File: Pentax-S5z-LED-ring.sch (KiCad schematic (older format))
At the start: 0 parts

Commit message: Placed a few traces.
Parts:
- added D1, D10, D11, D12, D13, D14, D15, D16, D2, D3, D4, D5, D6, D7, D8, D9: LED, symbol LED
- added R1, R10, R11, R12, R13, R14, R15, R16, R2, R3, R4, R5, R6, R7, R8, R9: 10R, symbol R
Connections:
- new net: D1.1 (A), D10.1 (A), D11.1 (A), D12.1 (A), D13.1 (A), D14.1 (A), D15.1 (A), D16.1 (A), D2.1 (A), D3.1 (A), D4.1 (A), D5.1 (A), D6.1 (A), D7.1 (A), D8.1 (A), D9.1 (A)
- new net: D1.2 (K), R1.1
- new net: D2.2 (K), R2.1
- new net: D3.2 (K), R3.1
- new net: D4.2 (K), R4.1
- new net: R1.2, R10.2, R11.2, R12.2, R13.2, R14.2, R15.2, R16.2, R2.2, R3.2, R4.2, R5.2, R6.2, R7.2, R8.2, R9.2
- new net: D5.2 (K), R5.1
- new net: D6.2 (K), R6.1
- new net: D7.2 (K), R7.1
- new net: D8.2 (K), R8.1
- new net: D9.2 (K), R9.1
- new net: D10.2 (K), R10.1
- new net: D11.2 (K), R11.1
- new net: D12.2 (K), R12.1
- new net: D13.2 (K), R13.1
- new net: D14.2 (K), R14.1
- new net: D15.2 (K), R15.1
- new net: D16.2 (K), R16.1

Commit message: Trying to build a controller board.
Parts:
- added IC1: ATTINY13-S, SO8-200, symbol ATTINY13-S
- added JP1: MADW__AVR_ISP, ~, symbol MADW__AVR_ISP
- added Q1: MOSFET_N, ~, symbol MOSFET_N
- added R17: 150R, symbol R
- added R18: 100k, symbol R
- added SW1, SW2: SW_PUSH, symbol SW_PUSH
- R1: value 10R -> 60R
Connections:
- net +5V: now reaches D1.1 (A), D10.1 (A), D11.1 (A), D12.1 (A), D13.1 (A), D14.1 (A), D15.1 (A), D16.1 (A), D2.1 (A), D3.1 (A), D4.1 (A), D5.1 (A), D6.1 (A), D7.1 (A), D8.1 (A), D9.1 (A)
- net +5V: now also IC1.8 (VCC), JP1.2 (VTG)
- net at R1.2, R10.2, R11.2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: now also Q1.3 (D)
- new net: Q1.1 (G), R17.2, R18.1
- new net GND: IC1.4 (GND), JP1.6 (GND), Q1.2 (S), R18.2, SW1.1, SW2.1
- new net MISO: IC1.6 (PB1(MISO/AIN1/OC0B/INT0/PCINT1)), JP1.1 (MISO), SW1.2
- new net PWM: IC1.5 (PB0(MOSI/AIN0/OC0A/PCINT0)), JP1.4 (MOSI), R17.1
- new net RESET: IC1.1 (PB5(~RESET~/ADC0/PCINT5/dW)), JP1.5 (RST)
- new net SCK: IC1.7 (PB2(SCK/ADC1/T0/PCINT2)), JP1.3 (SCK), SW2.2
- no-connect marks 0 -> 2
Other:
- moved on the sheet: D1, D10, D11, D12, D13, D14, D15, D16, D2, D3, D4, D5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

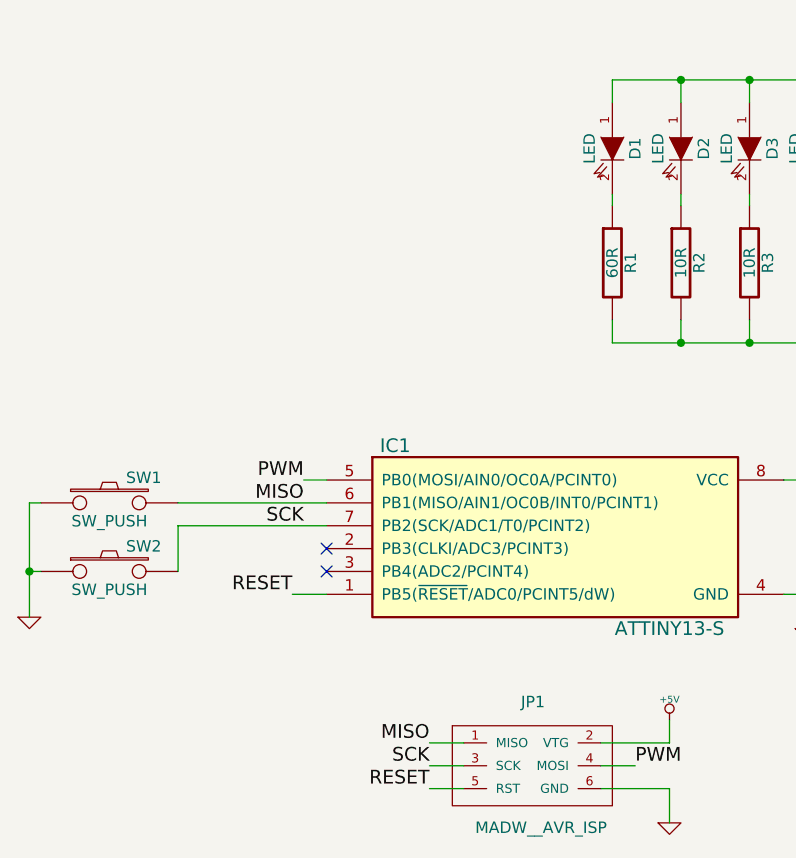
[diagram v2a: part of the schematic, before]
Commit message: Added proper SMD push-buttons.
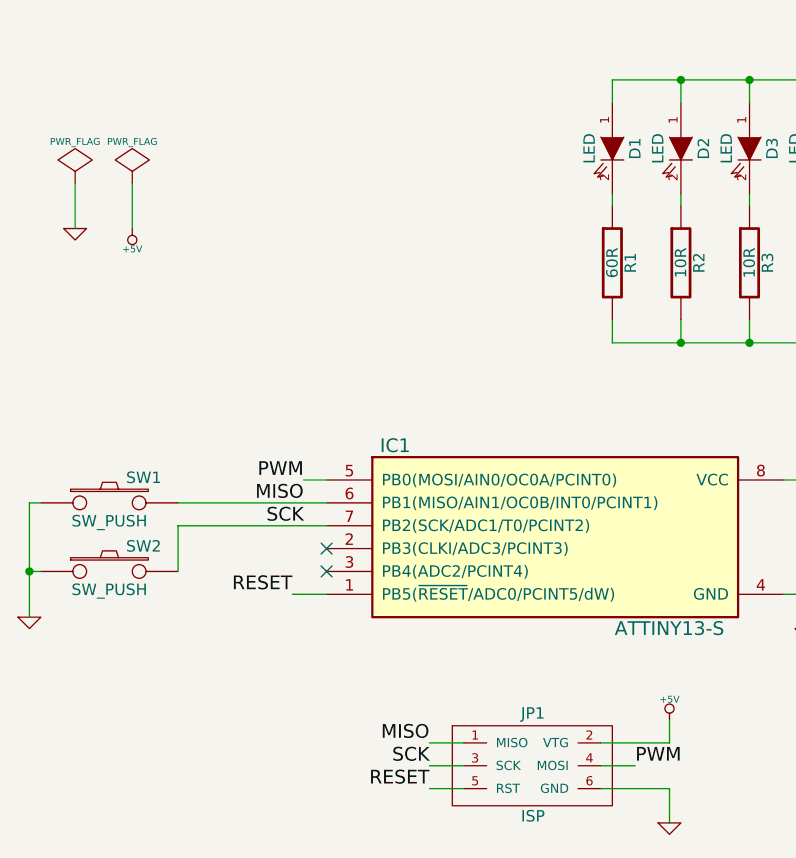
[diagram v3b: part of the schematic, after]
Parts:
- JP1: value MADW__AVR_ISP -> ISP
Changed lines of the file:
@@
-EESchema Schematic File Version 2  date Tue 09 Apr 2013 03:14:07 PM CEST
+EESchema Schematic File Version 2  date Tue 09 Apr 2013 06:31:30 PM CEST
 LIBS:my_parts
 LIBS:power
@@
 U 1 1 5164175A
 P 3200 5450
-F 0 "JP1" H 3150 5700 50  0000 L BNN
-F 1 "MADW__AVR_ISP" H 2950 5150 50  0000 L BNN
+F 0 "JP1" H 3150 5650 50  0000 L BNN
+F 1 "ISP" H 3150 5200 50  0000 L BNN
 F 2 "~" H 3200 5450 60  0000 C CNN
 F 3 "~" H 3200 5450 60  0000 C CNN
@@
 NoConn ~ 2300 4500
 NoConn ~ 2300 4600
+$Comp
+L GND #PWR09
+U 1 1 51644384
+P 1200 3100
+F 0 "#PWR09" H 1200 3100 30  0001 C CNN
+F 1 "GND" H 1200 3030 30  0001 C CNN
+F 2 "" H 1200 3100 60  0000 C CNN
+F 3 "" H 1200 3100 60  0000 C CNN
+	1    1200 3100
+	1    0    0    -1
+$EndComp
+$Comp
+L +5V #PWR010
+U 1 1 51644393
+P 1450 3100
+F 0 "#PWR010" H 1450 3190 20  0001 C CNN
+F 1 "+5V" H 1450 3190 30  0000 C CNN
+F 2 "" H 1450 3100 60  0000 C CNN
+F 3 "" H 1450 3100 60  0000 C CNN
+	1    1450 3100
+	-1   0    0    1
+$EndComp
+$Comp
+L PWR_FLAG #FLG011
+U 1 1 516443A2
+P 1200 2900
+F 0 "#FLG011" H 1200 2995 30  0001 C CNN
+F 1 "PWR_FLAG" H 1200 3080 30  0000 C CNN
+F 2 "" H 1200 2900 60  0000 C CNN
+F 3 "" H 1200 2900 60  0000 C CNN
+	1    1200 2900
+	1    0    0    -1
+$EndComp
+$Comp
+L PWR_FLAG #FLG012
+U 1 1 516443B1
+P 1450 2900
+F 0 "#FLG012" H 1450 2995 30  0001 C CNN
+F 1 "PWR_FLAG" H 1450 3080 30  0000 C CNN
+F 2 "" H 1450 2900 60  0000 C CNN
+F 3 "" H 1450 2900 60  0000 C CNN
+	1    1450 2900
+	1    0    0    -1
+$EndComp
+Wire Wire Line
+	1450 2900 1450 3100
+Wire Wire Line
+	1200 2900 1200 3100
 $EndSCHEMATC

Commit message: ...
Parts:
- added P1, P4: CONN_2, symbol CONN_2
- added P2: +, symbol CONN_1
- added P3: -, symbol CONN_1
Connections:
- net +5V: now also P1.1 (P1), P4.1 (P1); no longer D1.1 (A), D10.1 (A), D11.1 (A), D12.1 (A), D13.1 (A), D14.1 (A), D15.1 (A), D16.1 (A), D2.1 (A), D3.1 (A), D4.1 (A), D5.1 (A), D6.1 (A), D7.1 (A), D8.1 (A), D9.1 (A)
- net GND: now also P1.2 (PM)
- net at R1.2, R10.2, R11.2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: now also P3.1; no longer Q1.3 (D)
- new net: D1.1 (A), D10.1 (A), D11.1 (A), D12.1 (A), D13.1 (A), D14.1 (A), D15.1 (A), D16.1 (A), D2.1 (A), D3.1 (A), D4.1 (A), D5.1 (A), D6.1 (A), D7.1 (A), D8.1 (A), D9.1 (A), P2.1
- new net: P4.2 (PM), Q1.3 (D)
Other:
- note added: "To LED board"
- note added: "To power supply"
- moved on the sheet: D1, D10, D11, D12, D13, D14, D15, D16, D2, D3, D4, D5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

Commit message: Getting there...
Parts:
- added C1: 4.7µF, symbol C
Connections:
- net +5V: now also C1.1
- net GND: now also C1.2
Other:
- moved on the sheet: P1, P4, Q1, R17, R18
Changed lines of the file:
@@
-EESchema Schematic File Version 2  date Tue 09 Apr 2013 09:44:23 PM CEST
+EESchema Schematic File Version 2  date Wed 10 Apr 2013 12:16:09 AM CEST
 LIBS:my_parts
 LIBS:power
@@
 L R R17
 U 1 1 51640F23
-P 5150 4450
-F 0 "R17" V 5230 4450 50  0000 C CNN
-F 1 "150R" V 5150 4450 50  0000 C CNN
-F 2 "" H 5150 4450 60  0000 C CNN
-F 3 "" H 5150 4450 60  0000 C CNN
-	1    5150 4450
+P 6000 4450
+F 0 "R17" V 6080 4450 50  0000 C CNN
+F 1 "150R" V 6000 4450 50  0000 C CNN
+F 2 "" H 6000 4450 60  0000 C CNN
+F 3 "" H 6000 4450 60  0000 C CNN
+	1    6000 4450
 	0    -1   -1   0
 $EndComp
@@
 L R R18
 U 1 1 51640F32
-P 5450 4900
-F 0 "R18" V 5530 4900 50  0000 C CNN
-F 1 "100k" V 5450 4900 50  0000 C CNN
-F 2 "" H 5450 4900 60  0000 C CNN
-F 3 "" H 5450 4900 60  0000 C CNN
-	1    5450 4900
+P 6300 4900
+F 0 "R18" V 6380 4900 50  0000 C CNN
+F 1 "100k" V 6300 4900 50  0000 C CNN
+F 2 "" H 6300 4900 60  0000 C CNN
+F 3 "" H 6300 4900 60  0000 C CNN
+	1    6300 4900
 	1    0    0    -1
 $EndComp
@@
 L MOSFET_N Q1
 U 1 1 51640F6E
-P 5500 4450
-F 0 "Q1" H 5700 4740 60  0000 R CNN
-F 1 "MOSFET_N" H 5700 4350 60  0000 R CNN
-F 2 "~" H 5500 4450 60  0000 C CNN
-F 3 "~" H 5500 4450 60  0000 C CNN
-	1    5500 4450
-	1    0    0    -1
-$EndComp
-Wire Wire Line
-	5400 4450 5500 4450
-Wire Wire Line
-	5450 4450 5450 4650
-Connection ~ 5450 4450
+P 6350 4450
+F 0 "Q1" H 6550 4740 60  0000 R CNN
+F 1 "MOSFET_N" H 6550 4350 60  0000 R CNN
+F 2 "~" H 6350 4450 60  0000 C CNN
+F 3 "~" H 6350 4450 60  0000 C CNN
+	1    6350 4450
+	1    0    0    -1
+$EndComp
+Wire Wire Line
+	6250 4450 6350 4450
+Wire Wire Line
+	6300 4450 6300 4650
+Connection ~ 6300 4450
 $Comp
 L GND #PWR01
 U 1 1 51641037
-P 5450 5250
-F 0 "#PWR01" H 5450 5250 30  0001 C CNN
-F 1 "GND" H 5450 5180 30  0001 C CNN
-F 2 "" H 5450 5250 60  0000 C CNN
-F 3 "" H 5450 5250 60  0000 C CNN
-	1    5450 5250
-	1    0    0    -1
-$EndComp
-Wire Wire Line
-	5450 5150 5450 5250
-Wire Wire Line
-	5800 4550 5800 5250
+P 6300 5250
+F 0 "#PWR01" H 6300 5250 30  0001 C CNN
+F 1 "GND" H 6300 5180 30  0001 C CNN
+F 2 "" H 6300 5250 60  0000 C CNN
+F 3 "" H 6300 5250 60  0000 C CNN
+	1    6300 5250
+	1    0    0    -1
+$EndComp
+Wire Wire Line
+	6300 5150 6300 5250
+Wire Wire Line
+	6650 4550 6650 5250
 $Comp
 L GND #PWR02
 U 1 1 51641142
-P 5800 5250
-F 0 "#PWR02" H 5800 5250 30  0001 C CNN
-F 1 "GND" H 5800 5180 30  0001 C CNN
-F 2 "" H 5800 5250 60  0000 C CNN
-F 3 "" H 5800 5250 60  0000 C CNN
-	1    5800 5250
+P 6650 5250
+F 0 "#PWR02" H 6650 5250 30  0001 C CNN
+F 1 "GND" H 6650 5180 30  0001 C CNN
+F 2 "" H 6650 5250 60  0000 C CNN
+F 3 "" H 6650 5250 60  0000 C CNN
+	1    6650 5250
 	1    0    0    -1
 $EndComp
@@
 $EndComp
 Wire Wire Line
-	4300 4200 4400 4200
-Wire Wire Line
-	4400 4200 4400 4100
+	4400 4100 4400 4250
 $Comp
 L GND #PWR05
@@
 $EndComp
 Wire Wire Line
-	4300 4700 4400 4700
-Wire Wire Line
-	4400 4700 4400 4850
-Text Label 4800 4450 2    60   ~ 0
+	4400 4650 4400 4850
+Text Label 5650 4450 2    60   ~ 0
 PWM
 Wire Wire Line
-	4800 4450 4900 4450
+	5650 4450 5750 4450
 Text Label 2200 4200 2    60   ~ 0
 PWM
@@
 L GND #PWR09
 U 1 1 51644384
-P 6850 4800
-F 0 "#PWR09" H 6850 4800 30  0001 C CNN
-F 1 "GND" H 6850 4730 30  0001 C CNN
-F 2 "" H 6850 4800 60  0000 C CNN
-F 3 "" H 6850 4800 60  0000 C CNN
-	1    6850 4800
+P 5250 6250
+F 0 "#PWR09" H 5250 6250 30  0001 C CNN
+F 1 "GND" H 5250 6180 30  0001 C CNN
+F 2 "" H 5250 6250 60  0000 C CNN
+F 3 "" H 5250 6250 60  0000 C CNN
+	1    5250 6250
 	1    0    0    -1
 $EndComp
@@
 L +5V #PWR010
 U 1 1 51644393
-P 7100 4800
-F 0 "#PWR010" H 7100 4890 20  0001 C CNN
-F 1 "+5V" H 7100 4890 30  0000 C CNN
-F 2 "" H 7100 4800 60  0000 C CNN
-F 3 "" H 7100 4800 60  0000 C CNN
-	1    7100 4800
+P 5500 6250
+F 0 "#PWR010" H 5500 6340 20  0001 C CNN
+F 1 "+5V" H 5500 6340 30  0000 C CNN
+F 2 "" H 5500 6250 60  0000 C CNN
+F 3 "" H 5500 6250 60  0000 C CNN
+	1    5500 6250
 	-1   0    0    1
 $EndComp
@@
 L PWR_FLAG #FLG011
 U 1 1 516443A2
-P 6850 4600
-F 0 "#FLG011" H 6850 4695 30  0001 C CNN
-F 1 "PWR_FLAG" H 6850 4780 30  0000 C CNN
-F 2 "" H 6850 4600 60  0000 C CNN
-F 3 "" H 6850 4600 60  0000 C CNN
-	1    6850 4600
+P 5250 6050
+F 0 "#FLG011" H 5250 6145 30  0001 C CNN
+F 1 "PWR_FLAG" H 5250 6230 30  0000 C CNN
+F 2 "" H 5250 6050 60  0000 C CNN
+F 3 "" H 5250 6050 60  0000 C CNN
+	1    5250 6050
 	1    0    0    -1
 $EndComp
@@
 L PWR_FLAG #FLG012
 U 1 1 516443B1
-P 7100 4600
-F 0 "#FLG012" H 7100 4695 30  0001 C CNN
-F 1 "PWR_FLAG" H 7100 4780 30  0000 C CNN
-F 2 "" H 7100 4600 60  0000 C CNN
-F 3 "" H 7100 4600 60  0000 C CNN
-	1    7100 4600
-	1    0    0    -1
-$EndComp
-Wire Wire Line
-	7100 4600 7100 4800
-Wire Wire Line
-	6850 4600 6850 4800
+P 5500 6050
+F 0 "#FLG012" H 5500 6145 30  0001 C CNN
+F 1 "PWR_FLAG" H 5500 6230 30  0000 C CNN
+F 2 "" H 5500 6050 60  0000 C CNN
+F 3 "" H 5500 6050 60  0000 C CNN
+	1    5500 6050
+	1    0    0    -1
+$EndComp
+Wire Wire Line
+	5500 6050 5500 6250
+Wire Wire Line
+	5250 6050 5250 6250
 $Comp
 L CONN_2 P1
 U 1 1 51646D70
-P 7850 4550
-F 0 "P1" V 7800 4550 40  0000 C CNN
-F 1 "CONN_2" V 7900 4550 40  0000 C CNN
-F 2 "" H 7850 4550 60  0000 C CNN
-F 3 "" H 7850 4550 60  0000 C CNN
-	1    7850 4550
+P 6250 6000
+F 0 "P1" V 6200 6000 40  0000 C CNN
+F 1 "CONN_2" V 6300 6000 40  0000 C CNN
+F 2 "" H 6250 6000 60  0000 C CNN
+F 3 "" H 6250 6000 60  0000 C CNN
+	1    6250 6000
 	0    -1   -1   0
 $EndComp
@@
 L GND #PWR013
 U 1 1 51646D84
-P 7950 5000
-F 0 "#PWR013" H 7950 5000 30  0001 C CNN
-F 1 "GND" H 7950 4930 30  0001 C CNN
-F 2 "" H 7950 5000 60  0000 C CNN
-F 3 "" H 7950 5000 60  0000 C CNN
-	1    7950 5000
+P 6350 6450
+F 0 "#PWR013" H 6350 6450 30  0001 C CNN
+F 1 "GND" H 6350 6380 30  0001 C CNN
+F 2 "" H 6350 6450 60  0000 C CNN
+F 3 "" H 6350 6450 60  0000 C CNN
+	1    6350 6450
 	1    0    0    -1
 $EndComp
@@
 L +5V #PWR014
 U 1 1 51646D93
-P 7750 5000
-F 0 "#PWR014" H 7750 5090 20  0001 C CNN
-F 1 "+5V" H 7750 5090 30  0000 C CNN
-F 2 "" H 7750 5000 60  0000 C CNN
-F 3 "" H 7750 5000 60  0000 C CNN
-	1    7750 5000
+P 6150 6450
+F 0 "#PWR014" H 6150 6540 20  0001 C CNN
+F 1 "+5V" H 6150 6540 30  0000 C CNN
+F 2 "" H 6150 6450 60  0000 C CNN
+F 3 "" H 6150 6450 60  0000 C CNN
+	1    6150 6450
 	-1   0    0    1
 $EndComp
 Wire Wire Line
-	7750 4900 7750 5000
-Wire Wire Line
-	7950 4900 7950 5000
+	6150 6350 6150 6450
+Wire Wire Line
+	6350 6350 6350 6450
 $Comp
 L CONN_1 P2
@@
 L CONN_2 P4
 U 1 1 51647217
-P 6150 3800
-F 0 "P4" V 6100 3800 40  0000 C CNN
-F 1 "CONN_2" V 6200 3800 40  0000 C CNN
-F 2 "" H 6150 3800 60  0000 C CNN
-F 3 "" H 6150 3800 60  0000 C CNN
-	1    6150 3800
-	1    0    0    -1
-$EndComp
-Wire Wire Line
-	5800 3900 5800 4150
+P 7000 3800
+F 0 "P4" V 6950 3800 40  0000 C CNN
+F 1 "CONN_2" V 7050 3800 40  0000 C CNN
+F 2 "" H 7000 3800 60  0000 C CNN
+F 3 "" H 7000 3800 60  0000 C CNN
+	1    7000 3800
+	1    0    0    -1
+$EndComp
+Wire Wire Line
+	6650 3900 6650 4150
 $Comp
 L +5V #PWR?
 U 1 1 516472A6
-P 5800 3650
-F 0 "#PWR?" H 5800 3740 20  0001 C CNN
-F 1 "+5V" H 5800 3740 30  0000 C CNN
-F 2 "" H 5800 3650 60  0000 C CNN
-F 3 "" H 5800 3650 60  0000 C CNN
-	1    5800 3650
-	1    0    0    -1
-$EndComp
-Wire Wire Line
-	5800 3650 5800 3700
-Text Notes 8100 4600 0    60   ~ 0
+P 6650 3650
+F 0 "#PWR?" H 6650 3740 20  0001 C CNN
+F 1 "+5V" H 6650 3740 30  0000 C CNN
+F 2 "" H 6650 3650 60  0000 C CNN
+F 3 "" H 6650 3650 60  0000 C CNN
+	1    6650 3650
+	1    0    0    -1
+$EndComp
+Wire Wire Line
+	6650 3650 6650 3700
+Text Notes 6500 6050 0    60   ~ 0
 To power supply
-Text Notes 6300 3850 0    60   ~ 0
+Text Notes 7150 3850 0    60   ~ 0
 To LED board
+Connection ~ 4400 4200
+Connection ~ 4400 4700
+$Comp
+L C C1
+U 1 1 516492F3
+P 4400 4450
+F 0 "C1" H 4450 4550 50  0000 L CNN
+F 1 "4.7µF" H 4450 4350 50  0000 L CNN
+F 2 "" H 4400 4450 60  0000 C CNN
+F 3 "" H 4400 4450 60  0000 C CNN
+	1    4400 4450
+	1    0    0    -1
+$EndComp
+Wire Wire Line
+	4300 4200 4400 4200
+Wire Wire Line
+	4300 4700 4400 4700
 $EndSCHEMATC
